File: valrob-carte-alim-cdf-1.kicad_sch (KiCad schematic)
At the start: 39 parts, among them J1 USB_C_Receptacle_USB2.0_14P, J2 Conn_01x02, J3 Conn_01x04_Pin, SW1 SW_Push, SW2 SW_Push, SW3 SW_Push, U1 SN65HVD230, U2 ESP32-S3-WROOM-1

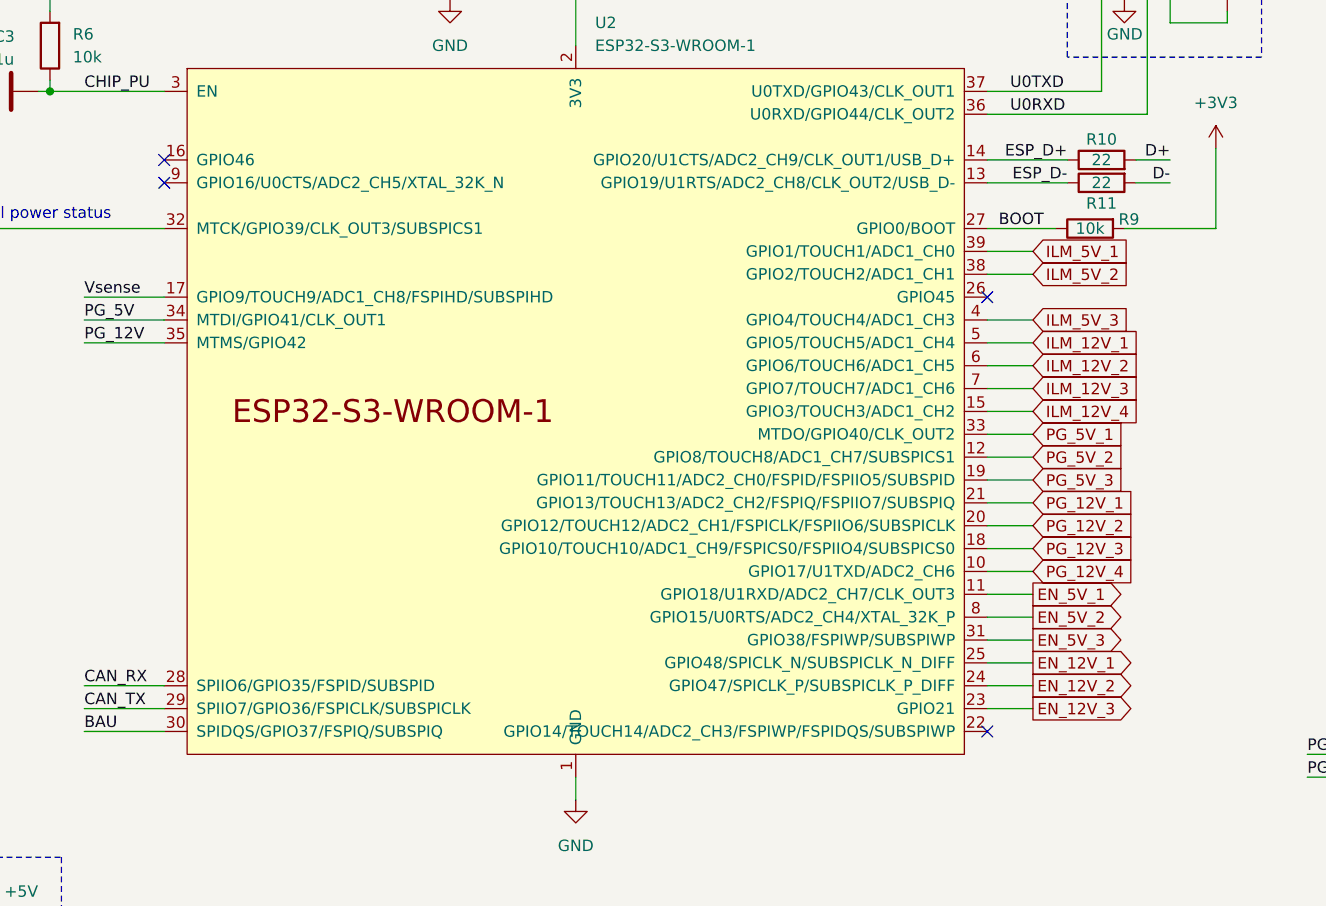
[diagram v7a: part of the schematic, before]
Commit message: schem: reorganize programmable gpios
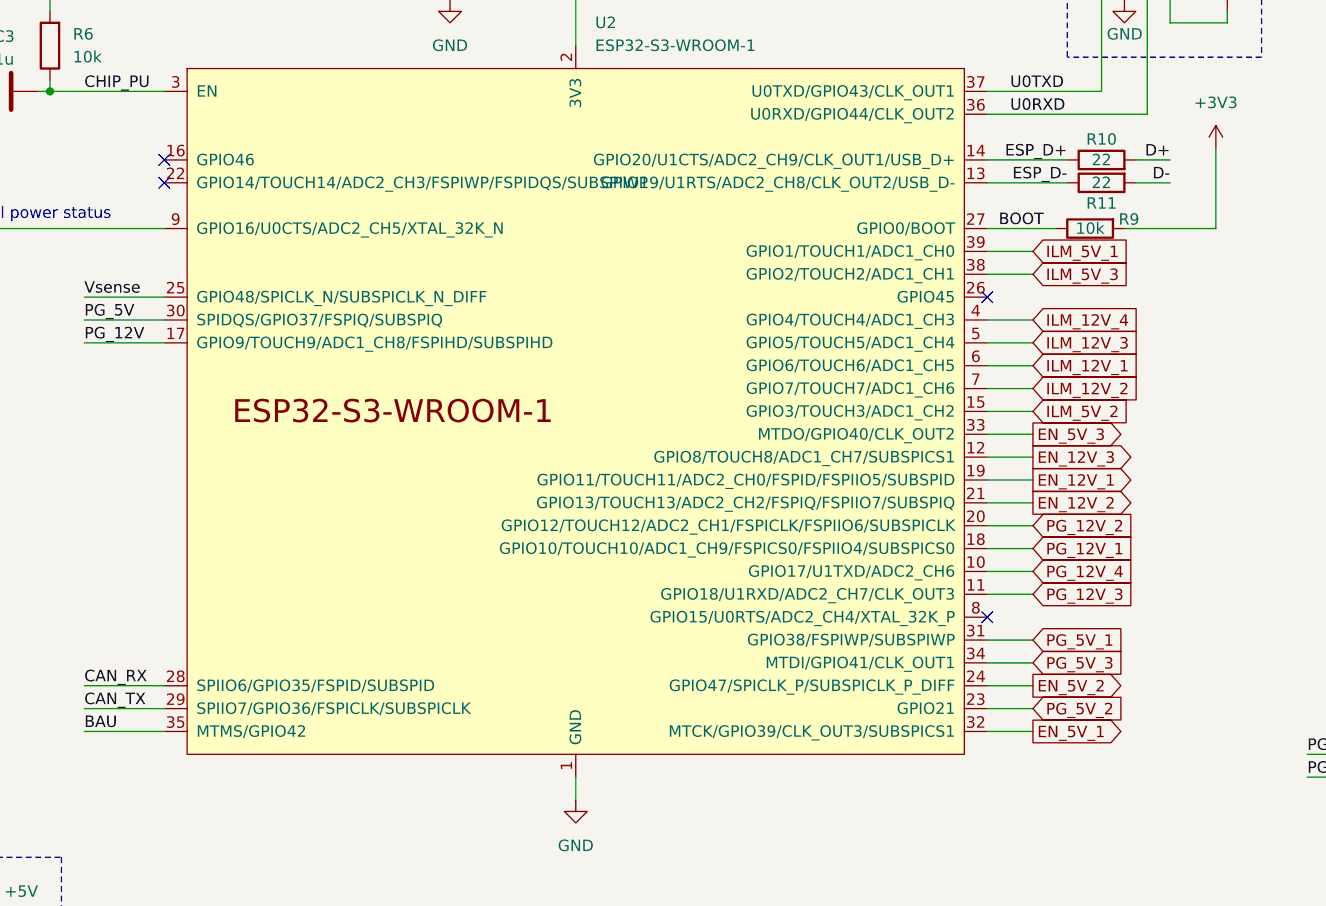
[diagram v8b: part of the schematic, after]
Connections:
- net BAU: now also U2.35 (MTMS/GPIO42); no longer U2.30 (SPIDQS/GPIO37/FSPIQ/SUBSPIQ)
- net EN_12V_1: now also U2.19 (GPIO11/TOUCH11/ADC2_CH0/FSPID/FSPIIO5/SUBSPID); no longer U2.25 (GPIO48/SPICLK_N/SUBSPICLK_N_DIFF)
- net EN_12V_2: now also U2.21 (GPIO13/TOUCH13/ADC2_CH2/FSPIQ/FSPIIO7/SUBSPIQ); no longer U2.24 (GPIO47/SPICLK_P/SUBSPICLK_P_DIFF)
- net EN_12V_3: now also U2.12 (GPIO8/TOUCH8/ADC1_CH7/SUBSPICS1); no longer U2.23 (GPIO21)
- net EN_5V_1: now also U2.32 (MTCK/GPIO39/CLK_OUT3/SUBSPICS1); no longer U2.11 (GPIO18/U1RXD/ADC2_CH7/CLK_OUT3)
- net EN_5V_2: now also U2.24 (GPIO47/SPICLK_P/SUBSPICLK_P_DIFF); no longer U2.8 (GPIO15/U0RTS/ADC2_CH4/XTAL_32K_P)
- net EN_5V_3: now also U2.33 (MTDO/GPIO40/CLK_OUT2); no longer U2.31 (GPIO38/FSPIWP/SUBSPIWP)
- net ILM_12V_1: now also U2.6 (GPIO6/TOUCH6/ADC1_CH5); no longer U2.5 (GPIO5/TOUCH5/ADC1_CH4)
- net ILM_12V_2: now also U2.7 (GPIO7/TOUCH7/ADC1_CH6); no longer U2.6 (GPIO6/TOUCH6/ADC1_CH5)
- net ILM_12V_3: now also U2.5 (GPIO5/TOUCH5/ADC1_CH4); no longer U2.7 (GPIO7/TOUCH7/ADC1_CH6)
- net ILM_12V_4: now also U2.4 (GPIO4/TOUCH4/ADC1_CH3); no longer U2.15 (GPIO3/TOUCH3/ADC1_CH2)
- net ILM_5V_2: now also U2.15 (GPIO3/TOUCH3/ADC1_CH2); no longer U2.38 (GPIO2/TOUCH2/ADC1_CH1)
- net ILM_5V_3: now also U2.38 (GPIO2/TOUCH2/ADC1_CH1); no longer U2.4 (GPIO4/TOUCH4/ADC1_CH3)
- net PG_12V: now also U2.17 (GPIO9/TOUCH9/ADC1_CH8/FSPIHD/SUBSPIHD); no longer U2.35 (MTMS/GPIO42)
- net PG_12V_1: now also U2.18 (GPIO10/TOUCH10/ADC1_CH9/FSPICS0/FSPIIO4/SUBSPICS0); no longer U2.21 (GPIO13/TOUCH13/ADC2_CH2/FSPIQ/FSPIIO7/SUBSPIQ)
- net PG_12V_3: now also U2.11 (GPIO18/U1RXD/ADC2_CH7/CLK_OUT3); no longer U2.18 (GPIO10/TOUCH10/ADC1_CH9/FSPICS0/FSPIIO4/SUBSPICS0)
- net PG_5V: now also U2.30 (SPIDQS/GPIO37/FSPIQ/SUBSPIQ); no longer U2.34 (MTDI/GPIO41/CLK_OUT1)
- net PG_5V_1: now also U2.31 (GPIO38/FSPIWP/SUBSPIWP); no longer U2.33 (MTDO/GPIO40/CLK_OUT2)
- net PG_5V_2: now also U2.23 (GPIO21); no longer U2.12 (GPIO8/TOUCH8/ADC1_CH7/SUBSPICS1)
- net PG_5V_3: now also U2.34 (MTDI/GPIO41/CLK_OUT1); no longer U2.19 (GPIO11/TOUCH11/ADC2_CH0/FSPID/FSPIIO5/SUBSPID)
- net Vsense: now also U2.25 (GPIO48/SPICLK_N/SUBSPICLK_N_DIFF); no longer U2.17 (GPIO9/TOUCH9/ADC1_CH8/FSPIHD/SUBSPIHD)
- net at D3.1 (K), D4.2 (A): now also U2.9 (GPIO16/U0CTS/ADC2_CH5/XTAL_32K_N); no longer U2.32 (MTCK/GPIO39/CLK_OUT3/SUBSPICS1)
